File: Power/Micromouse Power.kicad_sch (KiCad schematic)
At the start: 50 parts, among them J1 Battery, J2 Conn_02x08_Odd_Even, Q1 AO3401A, Q2 AO3401A, SW1 pwr, SW2 pwr, U1 AMS1117-3.3, U2 TP4056, U3 DRV8837, U4 DRV8837

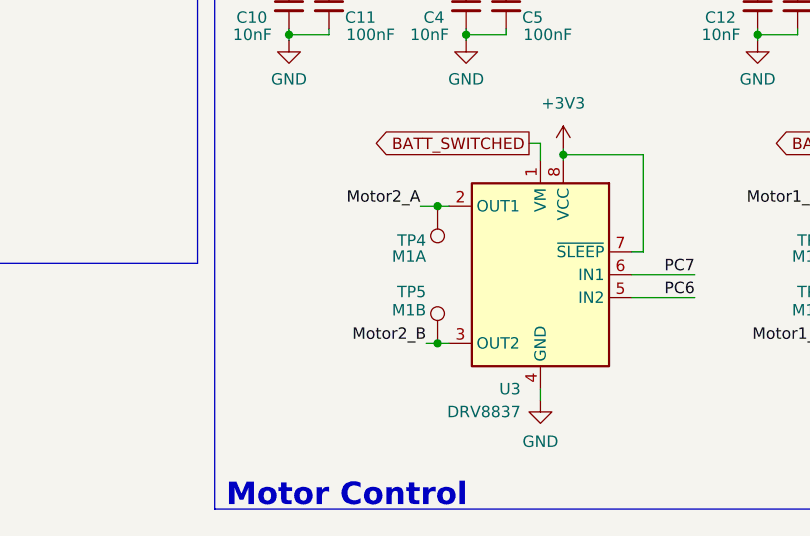
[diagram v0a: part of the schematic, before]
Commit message: Fixed M2 testpoints
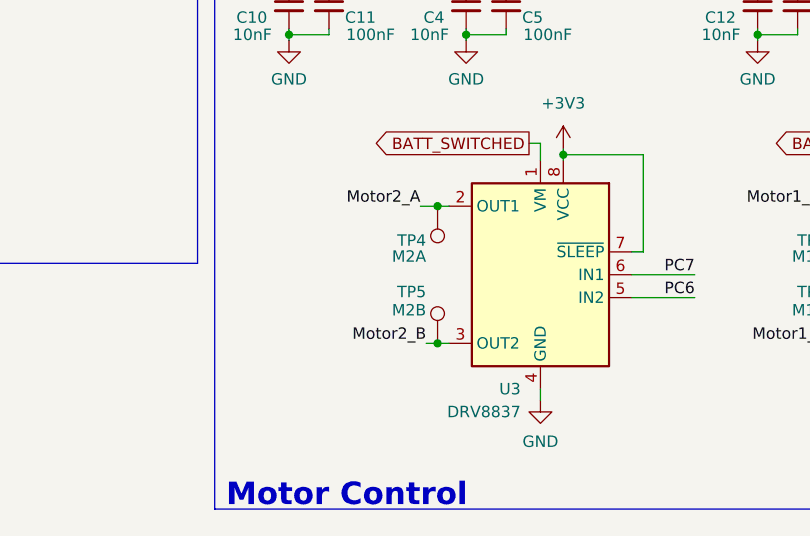
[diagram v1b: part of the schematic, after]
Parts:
- TP4: value M1A -> M2A
- TP5: value M1B -> M2B
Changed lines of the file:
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@@
       (effects (font (size 1.27 1.27)) (justify left))
     )
-    (property "Value" "M1A" (at 180.975 127.508 0)
+    (property "Value" "M2A" (at 180.975 127.508 0)
       (effects (font (size 1.27 1.27)) (justify left))
     )
@@
       (effects (font (size 1.27 1.27)) (justify left))
     )
-    (property "Value" "M1B" (at 180.975 133.477 0)
-      (effects (font (size 1.27 1.27)) (justify left))
-    )
+    (property "Value" "M2B" (at 180.975 133.477 0)
+      (effects (font (size 1.27 1.27)) (justify left))
+    )

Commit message: Final review and title info
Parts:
- added JP6: I_batt, Connector_PinHeader_2.54mm:PinHeader_1x02_P2.54mm_Vertical, symbol Jumper:Jumper_2_Bridged
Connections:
- net GND: now also JP6.2 (B); no longer J1.2 (Pin_2)
- new net: J1.2 (Pin_2), JP6.1 (A)
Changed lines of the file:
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@@
   (title_block
     (title "Micromouse Power")
-    (date "2024-03-21")
+    (date "2024-03-22")
     (rev "v0.0.0")
     (company "Group 55")
@@
     (stroke (width 0) (type default))
   )
+  (wire (pts (xy 67.945 22.86) (xy 69.85 22.86))
+    (stroke (width 0) (type default))
+  )
   (wire (pts (xy 240.665 116.205) (xy 249.555 116.205))
     (stroke (width 0) (type default))
@@
     (stroke (width 0) (type default))
   )
+  (wire (pts (xy 69.85 21.59) (xy 69.85 22.86))
+    (stroke (width 0) (type default))
+  )
   (wire (pts (xy 135.255 32.385) (xy 135.255 34.29))
     (stroke (width 0) (type default))
@@
     (stroke (width 0) (type default))
   )
-  (wire (pts (xy 67.945 22.86) (xy 69.215 22.86))
-    (stroke (width 0) (type default))
-  )
   (wire (pts (xy 185.42 93.98) (xy 185.42 96.52))
     (stroke (width 0) (type default))
@@
     (stroke (width 0) (type default))
   )
-  (wire (pts (xy 69.215 22.86) (xy 69.215 20.955))
-    (stroke (width 0) (type default))
-  )
   (wire (pts (xy 90.805 80.01) (xy 90.805 83.82))
     (stroke (width 0) (type default))
@@
     (stroke (width 0) (type default))
   )
-  (wire (pts (xy 69.215 25.4) (xy 69.215 28.575))
+  (wire (pts (xy 79.375 25.4) (xy 79.375 28.575))
     (stroke (width 0) (type default))
   )
@@
     )
   )
+  (symbol (lib_id "Jumper:Jumper_2_Bridged") (at 74.295 25.4 0) (unit 1)
+    (in_bom yes) (on_board yes) (dnp no)
+    (property "Reference" "JP6" (at 74.295 27.305 0)
+      (effects (font (size 1.27 1.27)) (justify right))
+    )
+    (property "Value" "I_batt" (at 76.2 29.21 0)
+      (effects (font (size 1.27 1.27)) (justify right))
+    )
+    (property "Footprint" "Connector_PinHeader_2.54mm:PinHeader_1x02_P2.54mm_Vertical" (at 74.295 25.4 0)
+      (effects (font (size 1.27 1.27)) hide)
+    )
+    (property "Datasheet" "~" (at 74.295 25.4 0)
+      (effects (font (size 1.27 1.27)) hide)
+    )
+    (property "Populate" "" (at 74.295 25.4 0)
+      (effects (font (size 1.27 1.27)) hide)
+    )
+    (pin "2")
+    (pin "1")
+    (instances
+      (project "Micromouse Power"
+        (path "/7a399d10-74ed-49ab-ab7d-478b1c564201"
+          (reference "JP6") (unit 1)
+        )
+      )
+    )
+  )
   (symbol (lib_id "Device:R_Small_US") (at 90.805 101.6 0) (mirror x) (unit 1)
     (in_bom yes) (on_board yes) (dnp no)
@@
     )
   )
-  (symbol (lib_id "power:GND") (at 69.215 28.575 0) (unit 1)
-    (in_bom yes) (on_board yes) (dnp no)
-    (property "Reference" "#PWR06" (at 69.215 34.925 0)
-      (effects (font (size 1.27 1.27)) hide)
-    )
-    (property "Value" "GND" (at 69.215 32.131 0)
-      (effects (font (size 1.27 1.27)))
-    )
-    (property "Footprint" "" (at 69.215 28.575 0)
-      (effects (font (size 1.27 1.27)) hide)
-    )
-    (property "Datasheet" "" (at 69.215 28.575 0)
+  (symbol (lib_id "power:GND") (at 79.375 28.575 0) (unit 1)
+    (in_bom yes) (on_board yes) (dnp no)
+    (property "Reference" "#PWR06" (at 79.375 34.925 0)
+      (effects (font (size 1.27 1.27)) hide)
+    )
+    (property "Value" "GND" (at 79.375 32.131 0)
+      (effects (font (size 1.27 1.27)))
+    )
+    (property "Footprint" "" (at 79.375 28.575 0)
+      (effects (font (size 1.27 1.27)) hide)
+    )
+    (property "Datasheet" "" (at 79.375 28.575 0)
       (effects (font (size 1.27 1.27)) hide)
     )
@@
     )
   )
-  (symbol (lib_id "power:+BATT") (at 69.215 20.955 0) (mirror y) (unit 1)
-    (in_bom yes) (on_board yes) (dnp no)
-    (property "Reference" "#PWR05" (at 69.215 24.765 0)
-      (effects (font (size 1.27 1.27)) hide)
-    )
-    (property "Value" "+BATT" (at 73.025 19.431 0)
-      (effects (font (size 1.27 1.27)))
-    )
-    (property "Footprint" "" (at 69.215 20.955 0)
-      (effects (font (size 1.27 1.27)) hide)
-    )
-    (property "Datasheet" "" (at 69.215 20.955 0)
-      (effects (font (size 1.27 1.27)) hide)
-    )
+  (symbol (lib_id "power:+BATT") (at 69.85 21.59 0) (mirror y) (unit 1)
+    (in_bom yes) (on_board yes) (dnp no)
+    (property "Reference" "#PWR05" (at 69.85 25.4 0)
+      (effects (font (size 1.27 1.27)) hide)
+    )
+    (property "Value" "+BATT" (at 73.66 20.066 0)
+      (effects (font (size 1.27 1.27)))
+    )
+    (property "Footprint" "" (at 69.85 21.59 0)
+      (effects (font (size 1.27 1.27)) hide)
+    )
+    (property "Datasheet" "" (at 69.85 21.59 0)
+      (effects (font (size 1.27 1.27)) hide)
+    )

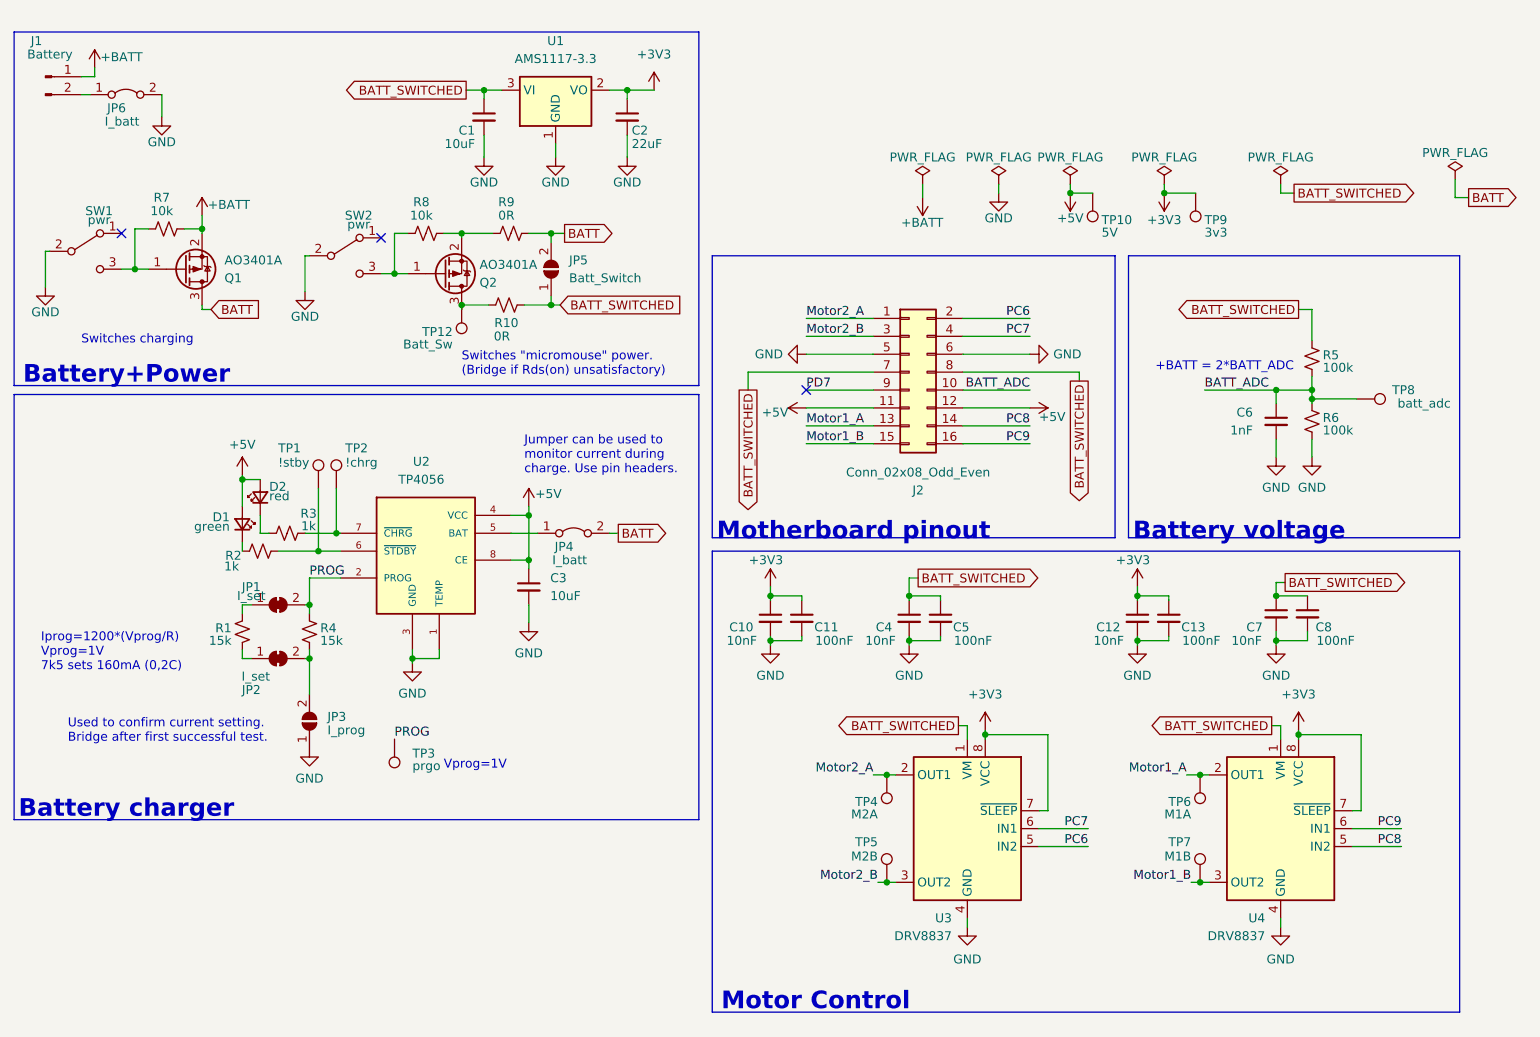
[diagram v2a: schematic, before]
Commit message: Added voltage divider for VCC
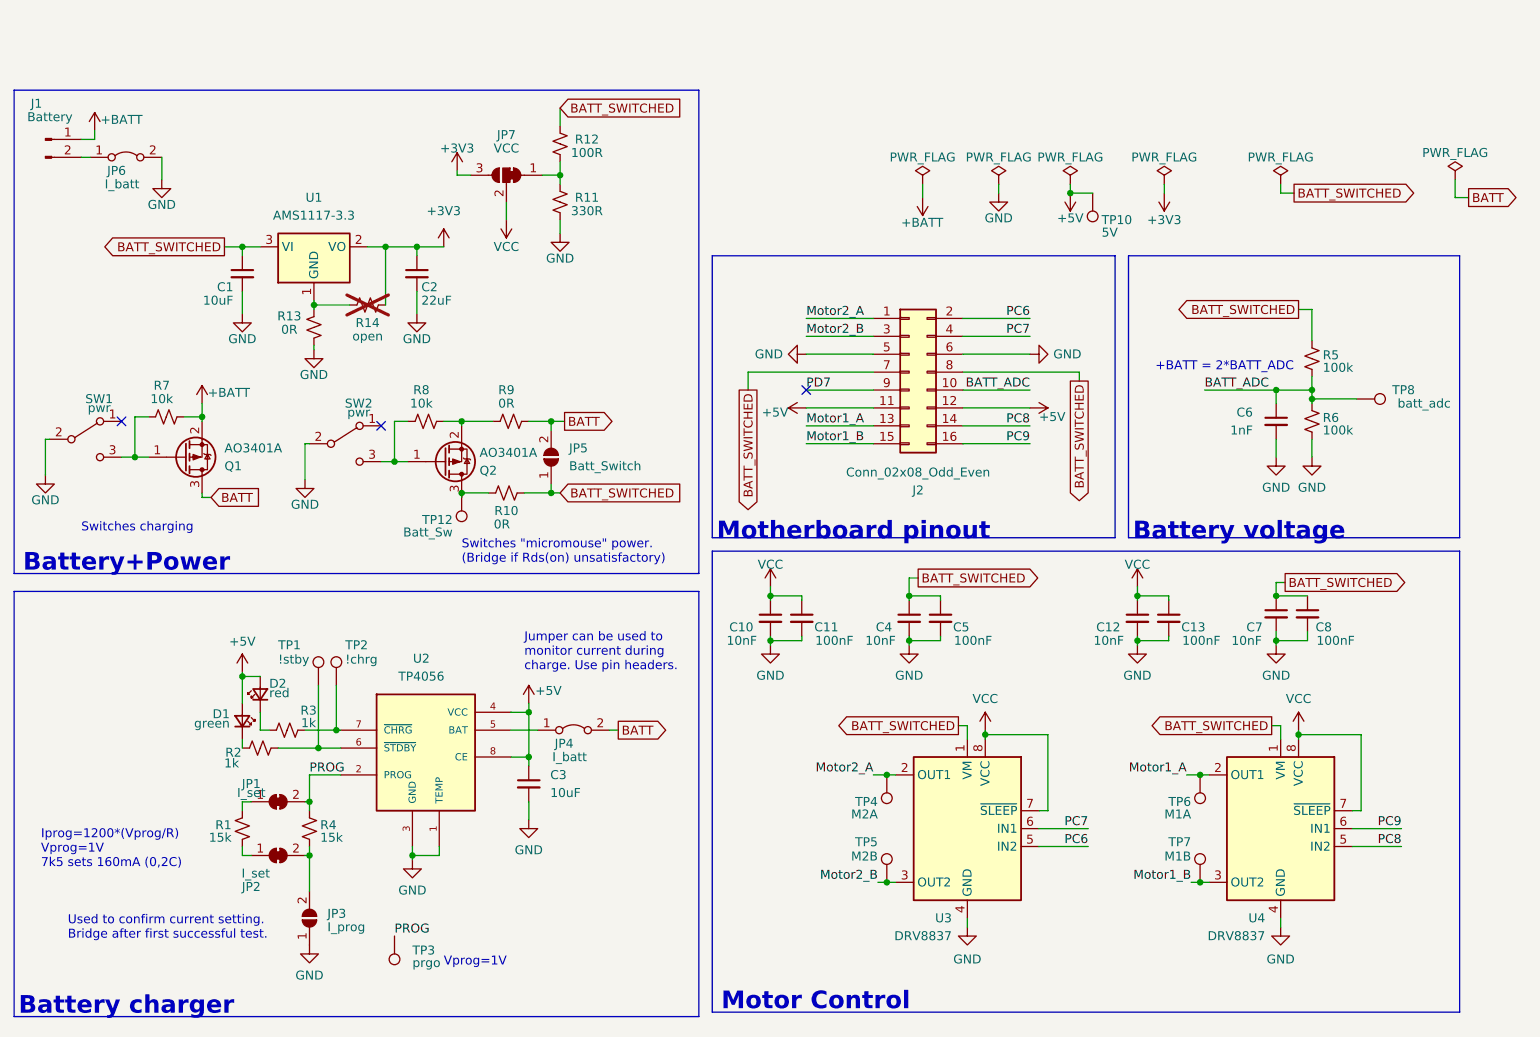
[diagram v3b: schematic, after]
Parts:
- removed TP9: 3v3, TestPoint:TestPoint_Pad_D1.0mm, symbol Connector:TestPoint
- added JP7: VCC, Jumper:SolderJumper-3_P1.3mm_Bridged12_Pad1.0x1.5mm_NumberLabels, symbol Jumper:SolderJumper_3_Bridged12
- added R11: 330R, Resistor_SMD:R_0603_1608Metric_Pad0.98x0.95mm_HandSolder, symbol Device:R_Small_US
- added R12: 100R, Resistor_SMD:R_0603_1608Metric_Pad0.98x0.95mm_HandSolder, symbol Device:R_Small_US
- added R13: 0R, Resistor_SMD:R_0603_1608Metric_Pad0.98x0.95mm_HandSolder, symbol Device:R_Small_US
- added R14: open, Resistor_SMD:R_0603_1608Metric_Pad0.98x0.95mm_HandSolder, symbol Device:R_Small_US
- C1, C3: LCSC (none) -> C19702
- C10, C12, C4, C7: LCSC (none) -> C57112
- C11, C13, C5, C8: LCSC (none) -> C14663
- C2: LCSC (none) -> C59461
- C6: LCSC (none) -> C1588
- D1: LCSC (none) -> C72038
- D2: LCSC (none) -> C2286
- Q1, Q2: LCSC (none) -> C15127
- R1, R4: LCSC (none) -> C17475
- R10, R9: LCSC (none) -> C21189
- R2, R3: LCSC (none) -> C21190
- R5, R6: LCSC (none) -> C25803
- R7, R8: LCSC (none) -> C25804
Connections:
- net +3V3: now also JP7.3 (B), R14.1; no longer C10.1, C11.1, C12.1, C13.1, U3.7 (~{SLEEP}), U3.8 (VCC), U4.7 (~{SLEEP}), U4.8 (VCC)
- net BATT_SWITCHED: now also R12.1
- net GND: now also R11.2, R13.1; no longer U1.1 (GND)
- new net: R13.2, R14.2, U1.1 (GND)
- new net: JP7.1 (A), R11.1, R12.2
- new net VCC: C10.1, C11.1, C12.1, C13.1, JP7.2 (C), U3.7 (~{SLEEP}), U3.8 (VCC), U4.7 (~{SLEEP}), U4.8 (VCC)
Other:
- moved on the sheet: C1, C2, C3, D1, D2, J1, JP1, JP2, JP3, JP4, JP5, JP6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

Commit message: Added comments for battery schematics
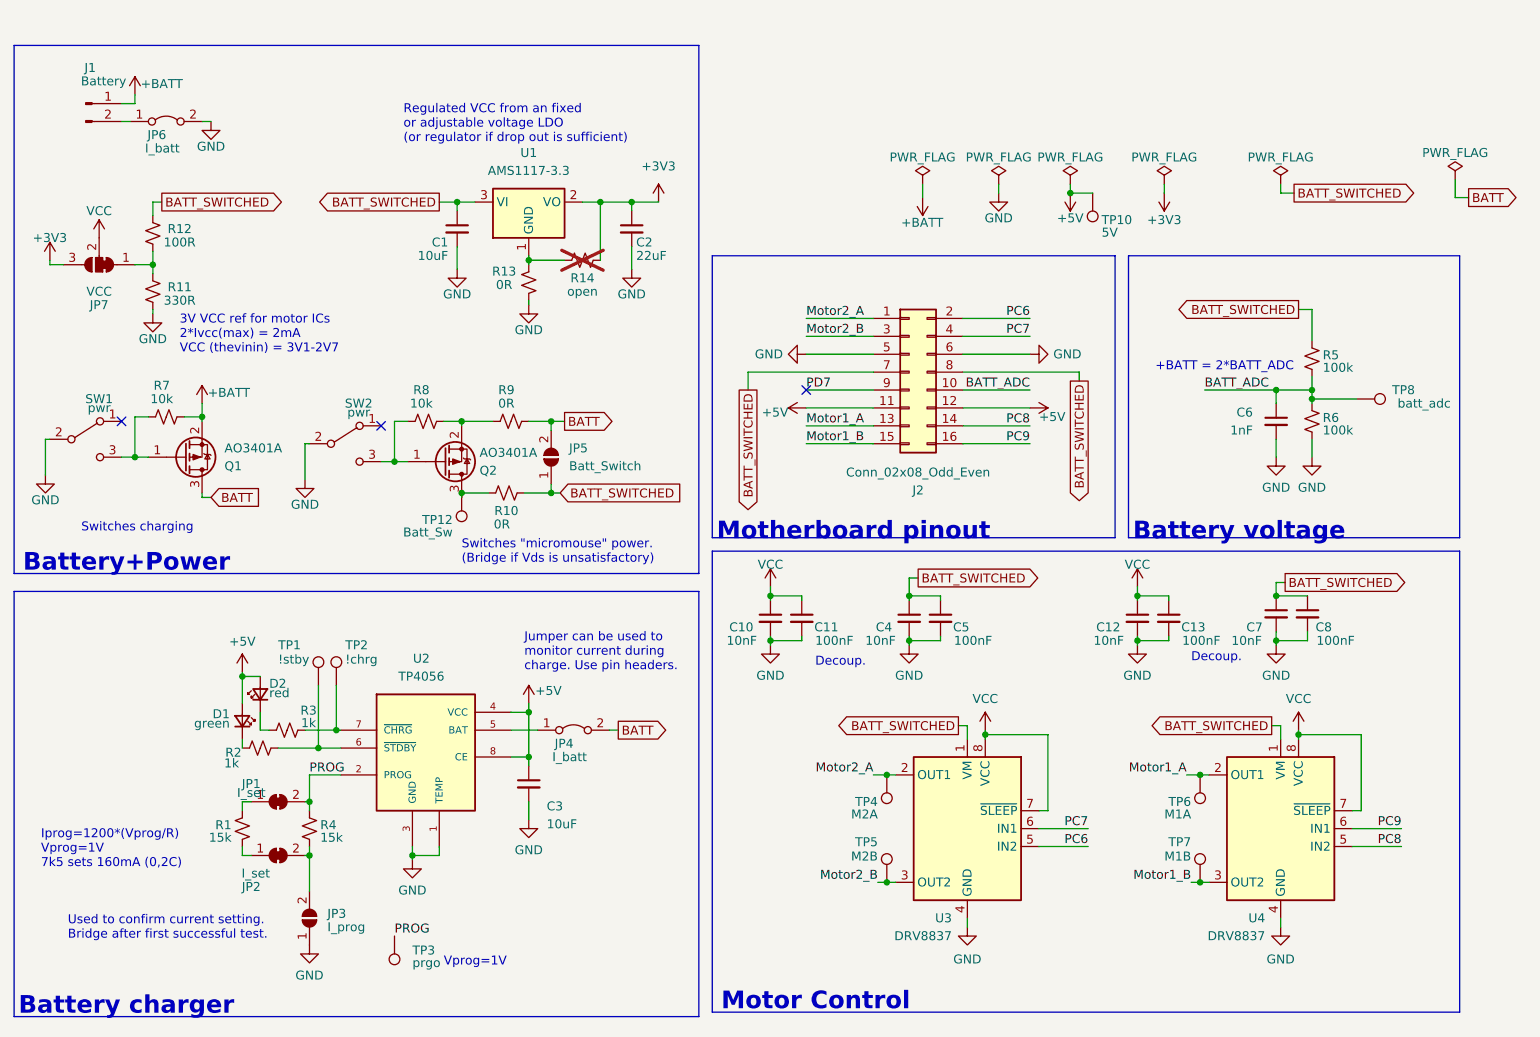
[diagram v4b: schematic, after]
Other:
- note added: "3V VCC ref for motor ICs 2*Ivcc(max) = 2mA VCC (thevinin) = 3V1-2V7"
- note added: "Decoup."
- note added: "Regulated VCC from an fixed or adjustable voltage LDO (or regulator if drop out is sufficient)"
- note added: "Switches "micromouse" power. (Bridge if Vds is unsatisfactory)"
- note removed: "Switches "micromouse" power. (Bridge if Rds(on) unsatisfactory)"
- moved on the sheet: C1, C2, J1, JP6, JP7, R11, R12, R13, R14, U1

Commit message: Updated schematic notes
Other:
- note added: "(Use JP7 to select between 3V ref and regulated 3V3)"
- note added: "*For adjustable regulator circuit"
- note added: "3V VCC ref for motor ICs 2*Ivcc(max) = 2mA As battery changes, VCC varies between 3V1-2V7"
- note added: "Battery current. Use Pin Header for ease of access."
- note added: "Highside switch to switch charging."
- note added: "Jumper can be used to monitor current during charge. Use pin headers for ease of access."
- note added: "Regulated VCC. Allows for a fixed or adjustable LDO (or regulator if drop out is sufficient). SOT-23."
- note added: "Switches "micromouse" power. Provides additional protection for loadsharing. (Bridge JP5 if Vds is significant)"
- note removed: "3V VCC ref for motor ICs 2*Ivcc(max) = 2mA VCC (thevinin) = 3V1-2V7"
- note removed: "Jumper can be used to monitor current during charge. Use pin headers."
- note removed: "Regulated VCC from an fixed or adjustable voltage LDO (or regulator if drop out is sufficient)"
- note removed: "Switches "micromouse" power. (Bridge if Vds is unsatisfactory)"
- note removed: "Switches charging"
- moved on the sheet: C1, C2, J1, JP5, JP6, JP7, Q1, Q2, R10, R11, R12, R13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
